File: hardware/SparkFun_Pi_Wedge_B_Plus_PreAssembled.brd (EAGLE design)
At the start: 73.7 x 63.5 mm, 15 parts

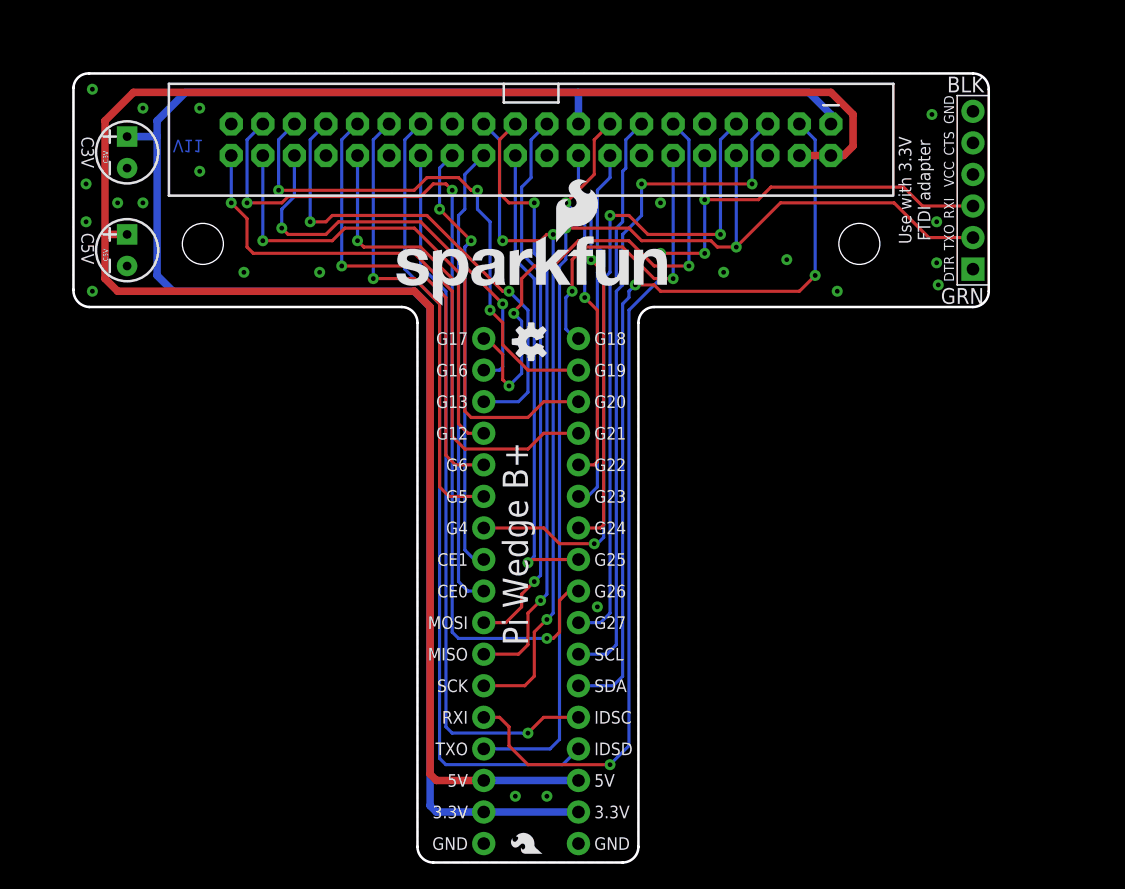
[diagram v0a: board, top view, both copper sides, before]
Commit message: Parts swapped, & old traces ripped up.
Ready for routing through the narrow neck.
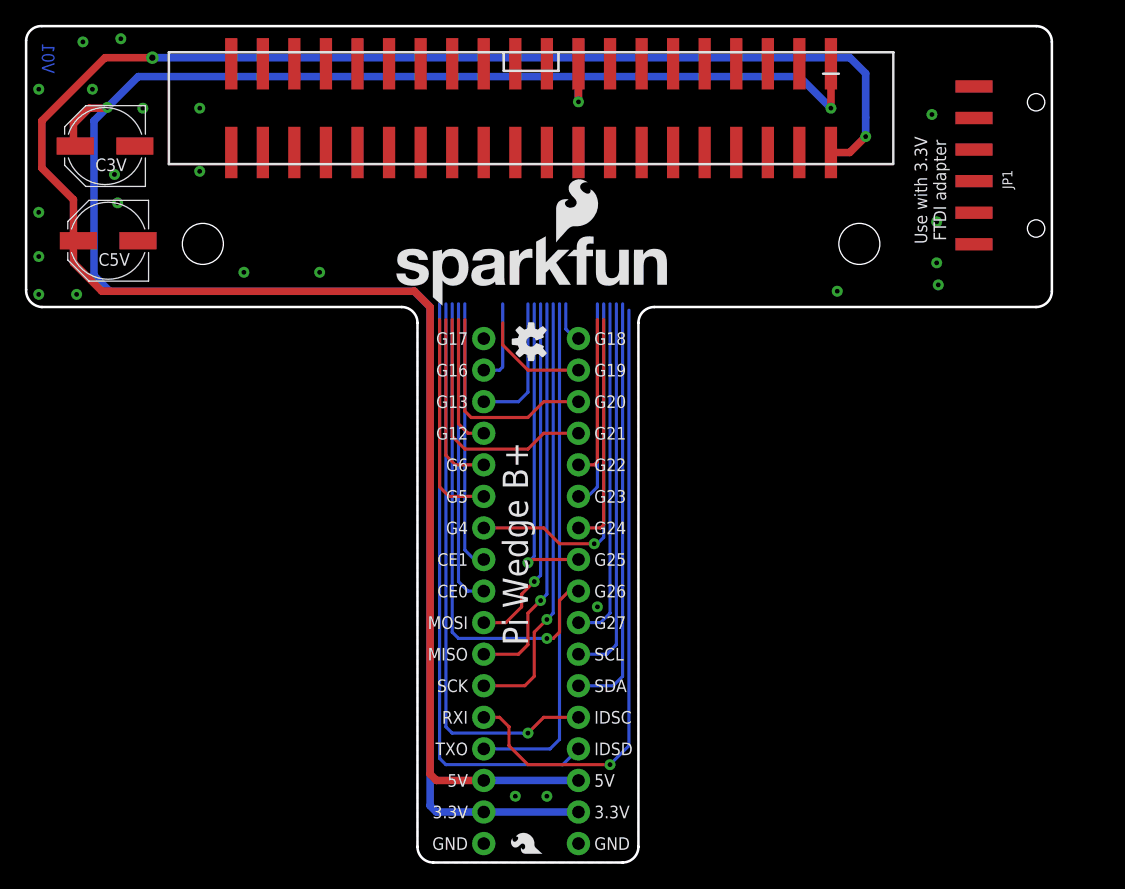
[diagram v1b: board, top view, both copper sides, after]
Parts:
- C3V, C5V: device SparkFun-Capacitors:CPOL-RADIAL-10UF-25V-KIT -> SparkFun-Capacitors:PANASONIC_D
- JP1: value FTDI_DEVICE -> FTDI_DEVICERA_SMT; device SparkFun-Connectors:FTDI_DEVICE_SIDE -> SparkFun-Connectors:FTDI_DEVICE_RA_SMT
- JP2: value RASPBERRYPI-B+-GPIO -> RASPBERRYPI-B+-GPIO-SMT; device SparkFun-Boards:2X20-SHROUDED -> SparkFun-Boards:2X20-SHROUDED-SMT
- moved JP1 5.46 mm to (77.5, 56.1)
- moved JP2 2.54 mm to (36.8, 60.7)
- moved U$2 2.54 mm to (36.8, 68.8)
- moved C3V 1.85 mm to (2.54, 57.7), turned to 180 degrees
- moved C5V 1.70 mm to (2.79, 50.0), turned to 180 degrees
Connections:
- net 3.3V: now also C3V.+; no longer C3V.1
- net 5V: now also C5V.+; no longer C5V.1
- net GND: now also C3V.-, C5V.-, JP1.6; no longer C3V.2, C5V.2, JP1.P$6
- net RXI: now also JP1.3; no longer JP1.P$3
- net TXO: now also JP1.2; no longer JP1.P$2
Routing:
- net TXO: track 91.2 -> 41.5 mm, vias 2 -> 0
- net GP17: track 41.9 -> 0.00 mm, vias 3 -> 0
- net RXI: track 89.5 -> 49.8 mm, vias 4 -> 1
- net GP19: track 42.9 -> 8.72 mm, vias 3 -> 0
- net GP26: track 73.2 -> 39.9 mm, vias 3 -> 1
- net SDA: track 63.7 -> 33.8 mm, vias 2 -> 0
- net GP13: track 39.8 -> 11.0 mm, vias 2 -> 0
- net GP20: track 45.8 -> 17.2 mm, vias 1 -> 0
- net GP21: track 48.7 -> 20.5 mm, vias 1 -> 0
- net GP16: track 34.1 -> 6.71 mm, vias 2 -> 0
- net GP4: track 55.4 -> 29.2 mm, vias 3 -> 1
- net SCL: track 55.5 -> 30.8 mm, vias 2 -> 0
- net GP18: track 26.6 -> 3.36 mm, vias 2 -> 0
- net GP6: track 37.5 -> 14.3 mm, vias 1 -> 0
- net GP5: track 37.8 -> 17.3 mm, vias 1 -> 0
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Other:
- board size 73.7 x 63.5 mm -> 82.5 x 67.3 mm
- board text added: "V01"
- board text removed: "C3V"
- board text removed: "C5V"
- board text removed: "V11"

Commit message: The hard part is routed.
Ready for Review.
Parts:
- moved FRAME2 9.43 mm to (19.6, -17.8)
- moved JP2 4.20 mm to (40.6, 58.9)
- moved STANDOFF2 4.07 mm to (67.3, 49.5)
- moved JP4 3.81 mm to (44.5, 1.52)
- moved LOGO2 3.81 mm to (51.8, 44.7)
- moved LOGO4 3.81 mm to (41.8, 2.67)
- moved LOGO5 3.81 mm to (40.6, 41.9)
- moved U$2 3.81 mm to (40.6, 68.8)
- moved C3V 3.81 mm to (6.35, 57.7)
- moved LOGO1 3.81 mm to (29.1, 44.7)
- moved JP3 3.81 mm to (36.8, 1.52)
- moved LOGO3 3.81 mm to (41.9, 0.38)
- moved STANDOFF1 3.57 mm to (14.0, 49.5)
- moved C5V 3.56 mm to (6.35, 50.0)
- moved JP1 3.14 mm to (80.5, 55.3)
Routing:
- net TXO: track 41.5 -> 89.2 mm, vias 0 -> 5
- net RXI: track 49.8 -> 95.0 mm, vias 1 -> 3
- net GP19: track 8.72 -> 47.8 mm, vias 0 -> 4
- net GP13: track 11.0 -> 49.6 mm, vias 0 -> 3
- net GP26: track 39.9 -> 75.4 mm, vias 1 -> 4
- net GP17: track 0.00 -> 35.3 mm, vias 0 -> 3
- net GP4: track 29.2 -> 62.1 mm, vias 1 -> 4
- net GP21: track 20.5 -> 50.0 mm
- net SDA: track 33.8 -> 63.1 mm, vias 0 -> 1
- net SCL: track 30.8 -> 58.5 mm, vias 0 -> 1
- net GP18: track 3.36 -> 30.8 mm, vias 0 -> 3
- net GP16: track 6.71 -> 33.9 mm, vias 0 -> 3
- net GP20: track 17.2 -> 43.8 mm, vias 0 -> 2
- net GP6: track 14.3 -> 39.4 mm, vias 0 -> 2
- net SCLK: track 35.0 -> 57.6 mm, vias 1 -> 4
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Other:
- board size 82.5 x 67.3 mm -> 82.5 x 65.5 mm
- board text added: "2x 0.13" holes Clear 4-40 screws"
- board text added: "All Units In Inches"
- board text added: "BLK"
- board text added: "GRN"

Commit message: A few touch-ups before review.
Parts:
- LOGO1: value SFE_LOGO_NAME_FLAME.2_INCH -> SFE_LOGO_NAME.2_INCH; device SparkFun-Aesthetics:SFE_LOGO_NAME_FLAME_.2 -> SparkFun-Aesthetics:SFE_LOGO_NAME_.2
- moved LOGO2 7.11 mm to (51.7, 51.8)
- moved C3V 1.52 mm to (6.35, 59.2)
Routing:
- net 3.3V: track 170.0 -> 168.8 mm
- net GP12: track 31.0 -> 30.2 mm
- net GP21: track 50.0 -> 50.7 mm
- net GP25: track 45.4 -> 44.9 mm

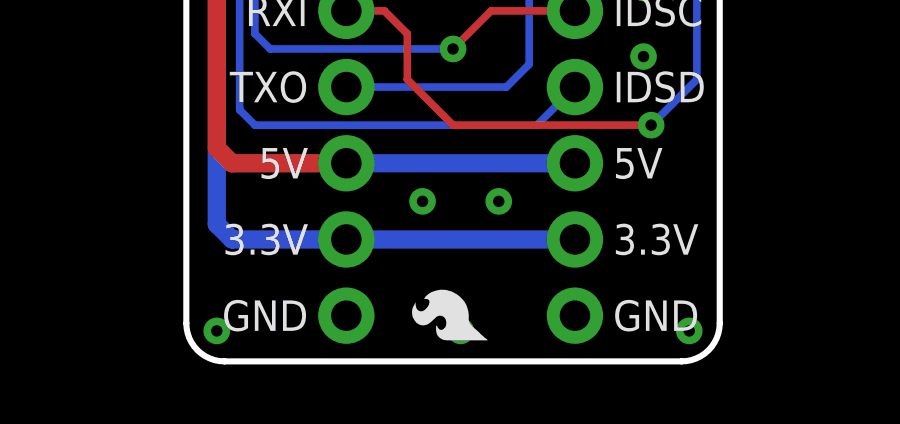
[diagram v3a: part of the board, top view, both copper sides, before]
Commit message: Added missing PROD_IDs.
Also apparently picked up huge changes from logo revamp in aesthetics
library.  This commit is huge, but with no physical changes to board or
schematic.
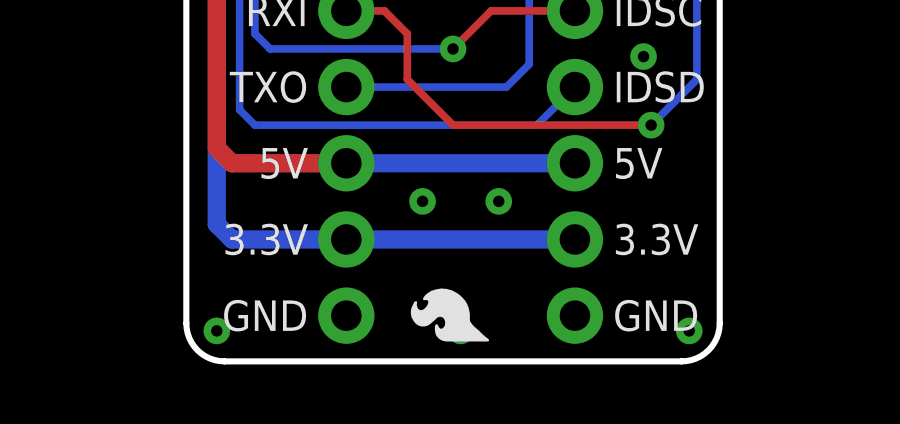
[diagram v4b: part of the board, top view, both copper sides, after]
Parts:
- JP3, JP4: value M17KIT -> (none)
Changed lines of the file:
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@@
 <setting verticaltext="up"/>
 </settings>
-<grid distance="0.01" unitdist="inch" unit="inch" style="lines" multiple="1" display="yes" altdistance="0.01" altunitdist="inch" altunit="inch"/>
+<grid distance="0.05" unitdist="inch" unit="inch" style="lines" multiple="1" display="yes" altdistance="0.005" altunitdist="inch" altunit="inch"/>
 <layers>
 <layer number="1" name="Top" color="4" fill="1" visible="yes" active="yes"/>
@@
 <layer number="19" name="Unrouted" color="6" fill="1" visible="yes" active="yes"/>
 <layer number="20" name="Dimension" color="15" fill="1" visible="yes" active="yes"/>
-<layer number="21" name="tPlace" color="16" fill="1" visible="no" active="yes"/>
-<layer number="22" name="bPlace" color="14" fill="1" visible="no" active="yes"/>
+<layer number="21" name="tPlace" color="16" fill="1" visible="yes" active="yes"/>
+<layer number="22" name="bPlace" color="14" fill="1" visible="yes" active="yes"/>
 <layer number="23" name="tOrigins" color="15" fill="1" visible="yes" active="yes"/>
 <layer number="24" name="bOrigins" color="15" fill="1" visible="yes" active="yes"/>
@@
 <layer number="37" name="tTest" color="7" fill="1" visible="no" active="yes"/>
 <layer number="38" name="bTest" color="7" fill="1" visible="no" active="yes"/>
-<layer number="39" name="tKeepout" color="4" fill="11" visible="yes" active="yes"/>
+<layer number="39" name="tKeepout" color="4" fill="11" visible="no" active="yes"/>
 <layer number="40" name="bKeepout" color="1" fill="11" visible="no" active="yes"/>
 <layer number="41" name="tRestrict" color="4" fill="10" visible="no" active="yes"/>
@@
 <layer number="45" name="Holes" color="7" fill="1" visible="yes" active="yes"/>
 <layer number="46" name="Milling" color="3" fill="1" visible="no" active="yes"/>
-<layer number="47" name="Measures" color="7" fill="1" visible="yes" active="yes"/>
+<layer number="47" name="Measures" color="7" fill="1" visible="no" active="yes"/>
 <layer number="48" name="Document" color="7" fill="1" visible="no" active="yes"/>
 <layer number="49" name="Reference" color="7" fill="1" visible="no" active="yes"/>
@@
 </element>
 <element name="U$2" library="SparkFun-Aesthetics" package="BREADBOARD_SPACING" value="BREADBOARD_PATTERN" x="40.64" y="68.834"/>
-<element name="JP2" library="SparkFun-Boards" package="2X20-SHROUDED-SMT" value="RASPBERRYPI-B+-GPIO-SMT" x="40.64" y="58.928" rot="R270"/>
-<element name="JP3" library="SparkFun-Connectors" package="1X17_NO_SILK_KIT" value="M17KIT" x="36.83" y="1.524" rot="MR90"/>
-<element name="JP4" library="SparkFun-Connectors" package="1X17_NO_SILK_KIT" value="M17KIT" x="44.45" y="1.524" rot="MR90"/>
+<element name="JP2" library="SparkFun-Boards" package="2X20-SHROUDED-SMT" value="RASPBERRYPI-B+-GPIO-SMT" x="40.64" y="58.928" rot="R270">
+<attribute name="PROD_ID" value="CONN-13143" x="40.64" y="58.928" size="1.778" layer="27" rot="R270" display="off"/>
+</element>
+<element name="JP3" library="SparkFun-Connectors" package="1X17_NO_SILK_KIT" value="" x="36.83" y="1.524" rot="MR90">
+<attribute name="PROD_ID" value="CONN-12294" x="36.83" y="1.524" size="1.778" layer="28" rot="MR90" display="off"/>
+</element>
+<element name="JP4" library="SparkFun-Connectors" package="1X17_NO_SILK_KIT" value="" x="44.45" y="1.524" rot="MR90">
+<attribute name="PROD_ID" value="CONN-12294" x="44.45" y="1.524" size="1.778" layer="28" rot="MR90" display="off"/>
+</element>
 <element name="LOGO2" library="SparkFun-Aesthetics" package="SFE_LOGO_NAME_FLAME_.2" value="SFE_LOGO_NAME_FLAME.2_INCH" x="51.689" y="51.816" rot="MR0"/>
 <element name="LOGO3" library="SparkFun-Aesthetics" package="SFE_LOGO_FLAME_.1" value="SFE_LOGO_FLAME.1_INCH" x="41.91" y="0.381" rot="R90"/>

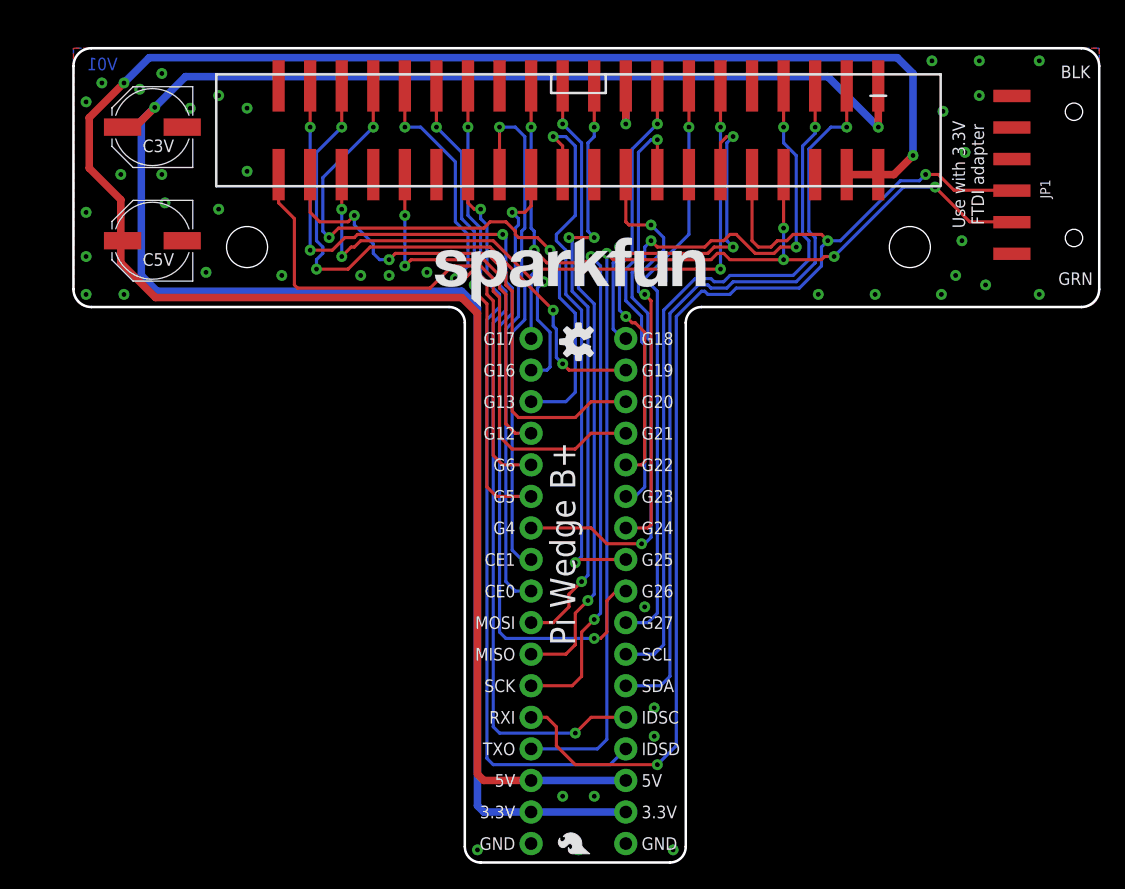
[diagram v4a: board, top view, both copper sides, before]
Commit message: Fixing review issues.
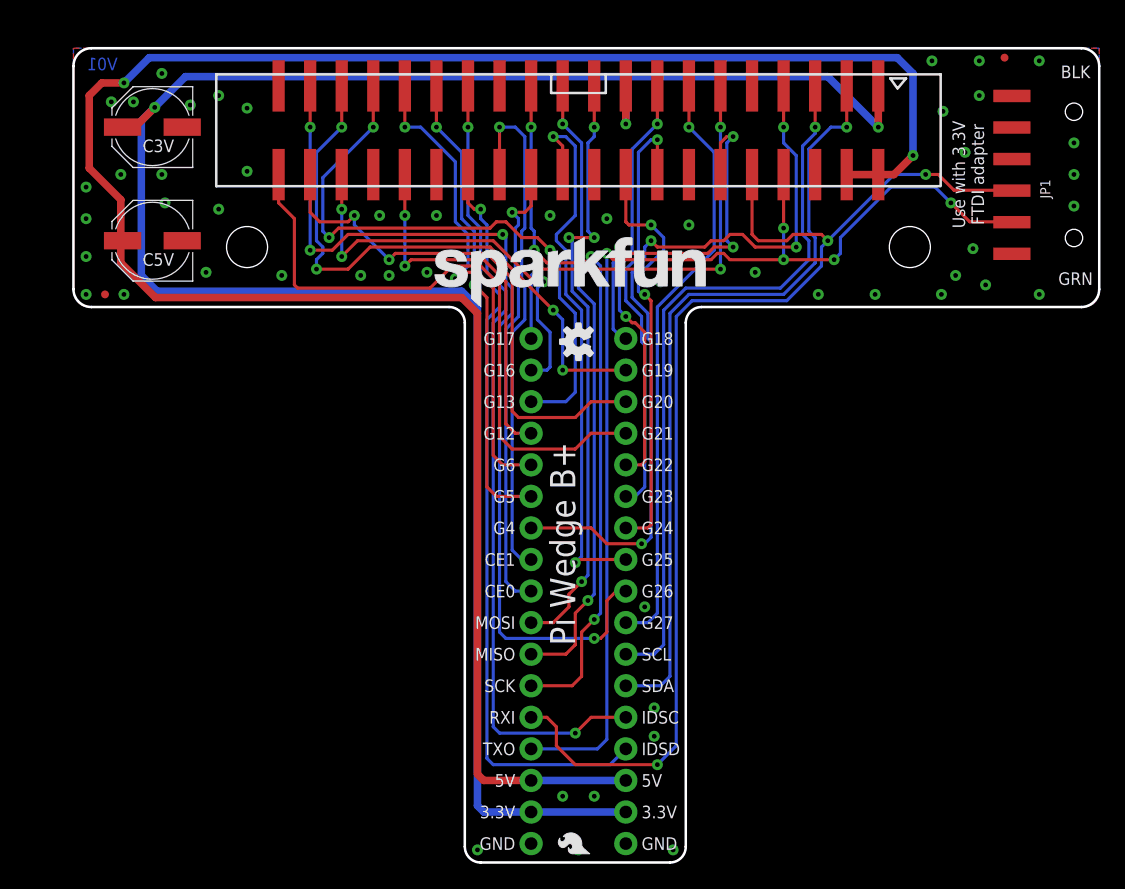
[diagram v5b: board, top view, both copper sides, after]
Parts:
- added FID1, FID2: FIDUCIALUFIDUCIAL, SparkFun-Aesthetics:MICRO-FIDUCIAL
- JP1: value FTDI_DEVICERA_SMT -> FTDI Device
- JP3, JP4: value (none) -> 1x17
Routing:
- net 5V: track 174.4 -> 175.5 mm
- net RXI: track 95.0 -> 94.0 mm
- net GP27: track 47.2 -> 48.0 mm
- net TXO: track 89.2 -> 89.9 mm
